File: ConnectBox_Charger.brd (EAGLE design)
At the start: 65 x 30 mm, 6 parts, among them J1 CONNECTOR_PI_40_PIN, J2 Lithium Cell, J3 microUSB Power In, J4 FTDI Serial, J5 5V Charger Output, U1 LTC4040

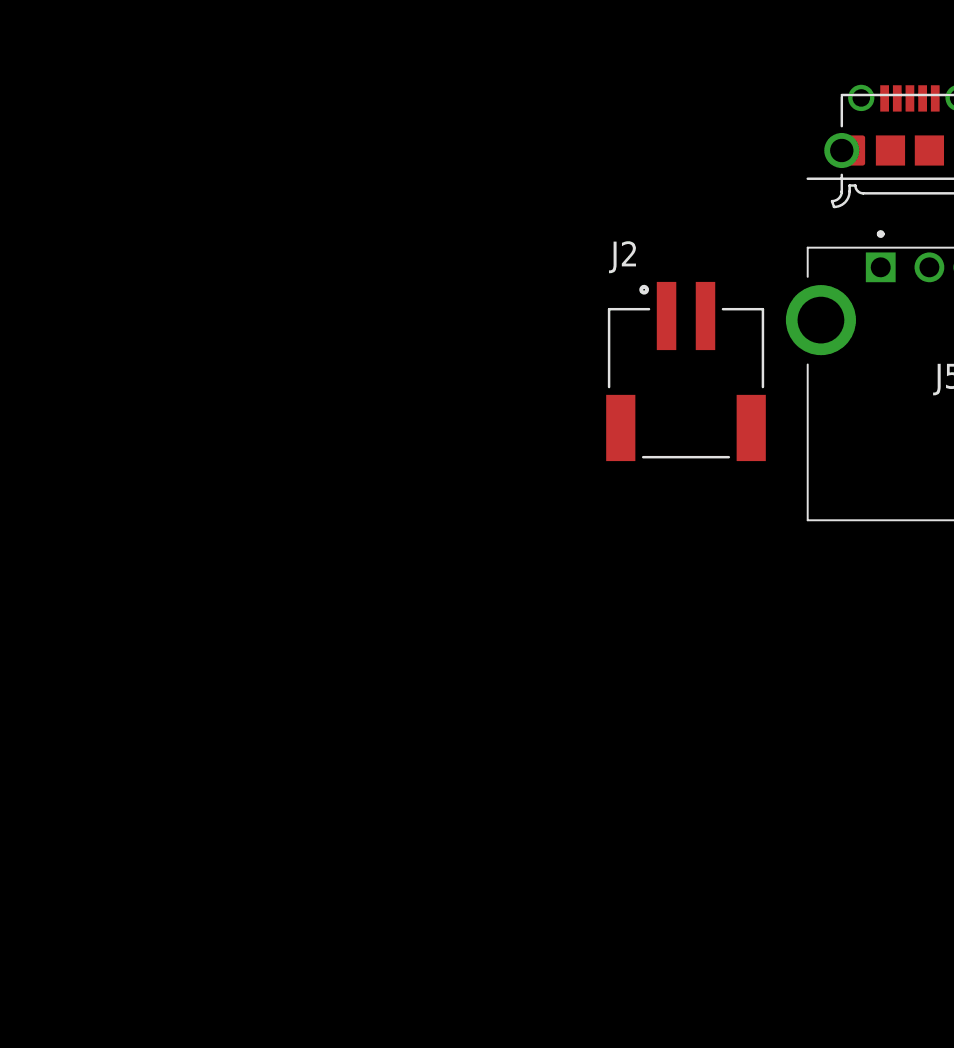
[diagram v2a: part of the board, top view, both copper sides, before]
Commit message: Add parts to library, Schematic. Add LTC4040 IC, inductor, 4x DIP switch, table of settings for Battery Chemistry, charging Voltage.
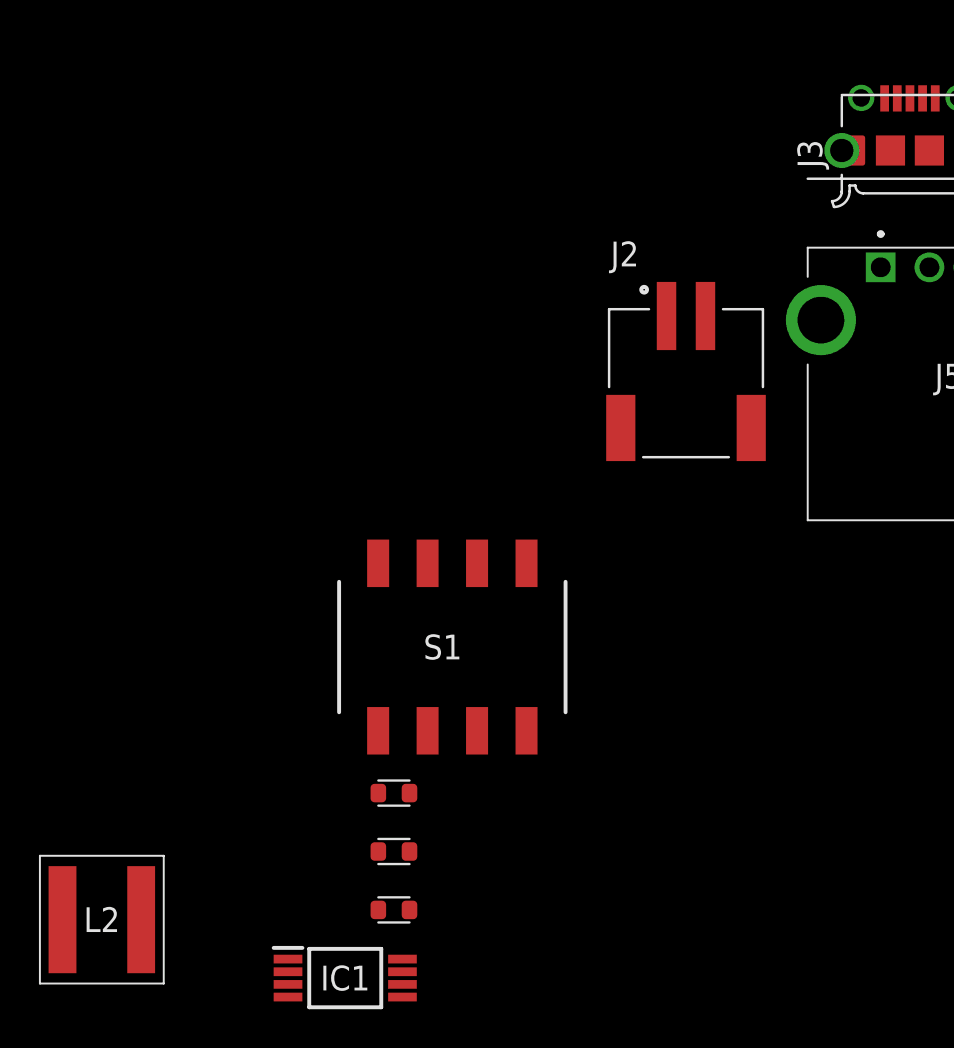
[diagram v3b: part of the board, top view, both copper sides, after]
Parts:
- added IC1: M24C32-RDW6TP, ConnectBox_2019:SOP65P640X120-8N
- added L2: XAL6030-182MEB, ConnectBox_2019:XAL6030182MEB
- added R1, R2, R3: (no value), ConnectBox_2019:RESC1608X55L25N
- added S1: configuration switches, ConnectBox_2019:219-4LPST
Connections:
- new net F0: R3.2, S1.3, U1.14
- new net F1: R2.2, S1.2, U1.13
- new net F2: R1.2, S1.1, U1.12
- net +5V: now also J1.2, J1.4
- net GND: now also R1.1, R2.1, R3.1, U1.17
- net V_IN: now also S1.5, S1.6, S1.7
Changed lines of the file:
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@@
 <attribute name="MF" value="FCI" x="-17.5" y="-25" size="1.778" layer="27" display="off"/>
 <attribute name="MP" value="10118194-0001LF" x="-17.5" y="-25" size="1.778" layer="27" display="off"/>
+<attribute name="NAME" x="-17.5" y="-24.365" size="2.54" layer="51" align="center"/>
 <attribute name="NAME" x="-22" y="-25.9" size="1.27" layer="25" rot="R90"/>
-<attribute name="NAME" x="-17.5" y="-24.365" size="2.54" layer="51" align="center"/>
 <attribute name="PACKAGE" value="DIP-4 FCI" x="-17.5" y="-25" size="1.778" layer="27" display="off"/>
 <attribute name="PRICE" value="0.24 USD" x="-17.5" y="-25" size="1.778" layer="27" display="off"/>
@@
 <attribute name="VALUE" x="-32.75341875" y="-43.6187" size="1.274540625" layer="27"/>
 </element>
+<element name="S1" library="ConnectBox_2019" package="219-4LPST" value="configuration switches" x="-41" y="-50.5" smashed="yes">
+<attribute name="DESCRIPTION" value="Series 219, SMD DIP-switch" x="-41" y="-50.5" size="1.778" layer="27" display="off"/>
+<attribute name="HEIGHT" value="mm" x="-41" y="-50.5" size="1.778" layer="27" display="off"/>
+<attribute name="MANUFACTURER_NAME" value="CTS" x="-41" y="-50.5" size="1.778" layer="27" display="off"/>
+<attribute name="MANUFACTURER_PART_NUMBER" value="219-4LPST" x="-41" y="-50.5" size="1.778" layer="27" display="off"/>
+<attribute name="MOUSER_PART_NUMBER" value="774-2194LPST" x="-41" y="-50.5" size="1.778" layer="27" display="off"/>
+<attribute name="MOUSER_PRICE-STOCK" value="https://www.mouser.com/Search/Refine.aspx?Keyword=774-2194LPST" x="-41" y="-50.5" size="1.778" layer="27" display="off"/>
+<attribute name="NAME" x="-41.492" y="-50.498" size="1.27" layer="25" align="center"/>
+<attribute name="RS_PART_NUMBER" value="1774220" x="-41" y="-50.5" size="1.778" layer="27" display="off"/>
+<attribute name="RS_PRICE-STOCK" value="http://uk.rs-online.com/web/p/products/1774220" x="-41" y="-50.5" size="1.778" layer="27" display="off"/>
+<attribute name="VALUE" x="-41.492" y="-50.498" size="1.27" layer="27" align="center"/>
+</element>
+<element name="R1" library="ConnectBox_2019" package="RESC1608X55L25N" value="" x="-44" y="-58" smashed="yes">
+<attribute name="NAME" x="-42.222" y="-58" size="1.524" layer="25" font="vector" ratio="10" align="center"/>
+<attribute name="NAME" x="-44" y="-58" size="1.016" layer="51" ratio="10" align="center"/>
+</element>
+<element name="R2" library="ConnectBox_2019" package="RESC1608X55L25N" value="" x="-44" y="-61" smashed="yes">
+<attribute name="NAME" x="-42.222" y="-61" size="1.524" layer="25" font="vector" ratio="10" align="center"/>
+<attribute name="NAME" x="-44" y="-61" size="1.016" layer="51" ratio="10" align="center"/>
+</element>
+<element name="R3" library="ConnectBox_2019" package="RESC1608X55L25N" value="" x="-44" y="-64" smashed="yes">
+<attribute name="NAME" x="-42.222" y="-64" size="1.524" layer="25" font="vector" ratio="10" align="center"/>
+<attribute name="NAME" x="-44" y="-64" size="1.016" layer="51" ratio="10" align="center"/>
+</element>
+<element name="IC1" library="ConnectBox_2019" package="SOP65P640X120-8N" value="M24C32-RDW6TP" x="-46.5" y="-67.5" smashed="yes">
+<attribute name="DESCRIPTION" value="STMICROELECTRONICS - M24C32-RDW6TP - EEPROM, 32KBIT, I2C, 1MHZ, TSSOP-8" x="-46.5" y="-67.5" size="1.778" layer="27" display="off"/>
+<attribute name="HEIGHT" value="1.2mm" x="-46.5" y="-67.5" size="1.778" layer="27" display="off"/>
+<attribute name="MANUFACTURER_NAME" value="STMicroelectronics" x="-46.5" y="-67.5" size="1.778" layer="27" display="off"/>
+<attribute name="MANUFACTURER_PART_NUMBER" value="M24C32-RDW6TP" x="-46.5" y="-67.5" size="1.778" layer="27" display="off"/>
+<attribute name="MOUSER_PART_NUMBER" value="511-M24C32-RDW6TP" x="-46.5" y="-67.5" size="1.778" layer="27" display="off"/>
+<attribute name="MOUSER_PRICE-STOCK" value="https://www.mouser.com/Search/Refine.aspx?Keyword=511-M24C32-RDW6TP" x="-46.5" y="-67.5" size="1.778" layer="27" display="off"/>
+<attribute name="NAME" x="-46.5" y="-67.5" size="1.27" layer="25" align="center"/>
+<attribute name="RS_PART_NUMBER" value="" x="-46.5" y="-67.5" size="1.778" layer="27" display="off"/>
+<attribute name="RS_PRICE-STOCK" value="" x="-46.5" y="-67.5" size="1.778" layer="27" display="off"/>
+<attribute name="VALUE" x="-46.5" y="-67.5" size="1.27" layer="27" align="center"/>
+</element>
+<element name="L2" library="ConnectBox_2019" package="XAL6030182MEB" value="XAL6030-182MEB" x="-59" y="-64.5" smashed="yes">
+<attribute name="DESCRIPTION" value="Fixed Inductors 1.8uH 20% 14A 10.52mOhms AEC-Q200" x="-59" y="-64.5" size="1.778" layer="27" display="off"/>
+<attribute name="HEIGHT" value="3.1mm" x="-59" y="-64.5" size="1.778" layer="27" display="off"/>
+<attribute name="MANUFACTURER_NAME" value="COILCRAFT" x="-59" y="-64.5" size="1.778" layer="27" display="off"/>
+<attribute name="MANUFACTURER_PART_NUMBER" value="XAL6030-182MEB" x="-59" y="-64.5" size="1.778" layer="27" display="off"/>
+<attribute name="MOUSER_PART_NUMBER" value="994-XAL6030-182MEB" x="-59" y="-64.5" size="1.778" layer="27" display="off"/>
+<attribute name="MOUSER_PRICE-STOCK" value="https://www.mouser.com/Search/Refine.aspx?Keyword=994-XAL6030-182MEB" x="-59" y="-64.5" size="1.778" layer="27" display="off"/>
+<attribute name="NAME" x="-59" y="-64.5" size="1.27" layer="25" align="center"/>
+<attribute name="RS_PART_NUMBER" value="" x="-59" y="-64.5" size="1.778" layer="27" display="off"/>
+<attribute name="RS_PRICE-STOCK" value="" x="-59" y="-64.5" size="1.778" layer="27" display="off"/>
+<attribute name="VALUE" x="-59" y="-64.5" size="1.27" layer="27" align="center"/>
+</element>
 </elements>
 <signals>
@@
 <contactref element="J5" pad="4"/>
 <contactref element="J2" pad="2"/>
-<wire x1="38.85" y1="25.23" x2="56.63" y2="25.23" width="0" layer="19" extent="1-1"/>
-<wire x1="18.53" y1="25.23" x2="38.85" y2="25.23" width="0" layer="19" extent="1-1"/>
-<wire x1="-20.5" y1="-0.5" x2="18.53" y2="25.23" width="0" layer="19" extent="1-1"/>
-<wire x1="-20.5" y1="-12" x2="-20.5" y2="-0.5" width="0" layer="19" extent="1-1"/>
-<wire x1="-16.2" y1="-22.325" x2="-20.5" y2="-12" width="0" layer="19" extent="1-1"/>
-<wire x1="-12" y1="-31" x2="-16.2" y2="-22.325" width="0" layer="19" extent="1-1"/>
-<wire x1="-8.93" y1="-33.71" x2="-12" y2="-31" width="0" layer="19" extent="1-1"/>
-<wire x1="-28" y1="-33.5" x2="-22.07" y2="-33.71" width="0" layer="19" extent="1-1"/>
+<contactref element="U1" pad="17"/>
+<contactref element="R3" pad="1"/>
+<contactref element="R2" pad="1"/>
+<contactref element="R1" pad="1"/>
+<wire x1="-44.8" y1="-61" x2="-44.8" y2="-64" width="0" layer="19" extent="1-1"/>
+<wire x1="-44.8" y1="-58" x2="-44.8" y2="-61" width="0" layer="19" extent="1-1"/>
+<wire x1="-28" y1="-33.5" x2="-44.8" y2="-58" width="0" layer="19" extent="1-1"/>
+<wire x1="-22.07" y1="-33.71" x2="-28" y2="-33.5" width="0" layer="19" extent="1-1"/>
+<wire x1="-12" y1="-31" x2="-8.93" y2="-33.71" width="0" layer="19" extent="1-1"/>
+<wire x1="-16.2" y1="-22.325" x2="-12" y2="-31" width="0" layer="19" extent="1-1"/>
+<wire x1="-20.5" y1="-12" x2="-16.2" y2="-22.325" width="0" layer="19" extent="1-1"/>
+<wire x1="-20.5" y1="-0.5" x2="-20.5" y2="-12" width="0" layer="19" extent="1-1"/>
+<wire x1="-18.565" y1="0" x2="-20.5" y2="-0.5" width="0" layer="19" extent="1-1"/>
+<wire x1="18.53" y1="25.23" x2="-18.565" y2="0" width="0" layer="19" extent="1-1"/>
+<wire x1="38.85" y1="25.23" x2="18.53" y2="25.23" width="0" layer="19" extent="1-1"/>
+<wire x1="56.63" y1="25.23" x2="38.85" y2="25.23" width="0" layer="19" extent="1-1"/>
 </signal>
 <signal name="TO_PI">
@@
 <signal name="V_IN">
 <contactref element="J3" pad="1"/>
+<contactref element="S1" pad="7"/>
+<contactref element="S1" pad="5"/>
+<contactref element="S1" pad="6"/>
+<wire x1="-39.73" y1="-46.2" x2="-42.27" y2="-46.2" width="0" layer="19" extent="1-1"/>
+<wire x1="-37.19" y1="-46.2" x2="-39.73" y2="-46.2" width="0" layer="19" extent="1-1"/>
+<wire x1="-18.8" y1="-22.325" x2="-37.19" y2="-46.2" width="0" layer="19" extent="1-1"/>
 </signal>
 <signal name="+5V">
 <contactref element="J5" pad="1"/>
+<contactref element="J1" pad="4"/>
+<contactref element="J1" pad="2"/>
+<wire x1="8.37" y1="27.77" x2="-19" y2="-31" width="0" layer="19" extent="1-1"/>
+<wire x1="10.91" y1="27.77" x2="8.37" y2="27.77" width="0" layer="19" extent="1-1"/>
 </signal>
 <signal name="BATT">
 <contactref element="J2" pad="1"/>
 </signal>
+<signal name="F2">
+<contactref element="U1" pad="12"/>
+<contactref element="S1" pad="1"/>
+<contactref element="R1" pad="2"/>
+<wire x1="-44.81" y1="-54.8" x2="-43.2" y2="-58" width="0" layer="19" extent="1-1"/>
+<wire x1="-19.5" y1="-2.935" x2="-44.81" y2="-54.8" width="0" layer="19" extent="1-1"/>
+</signal>
+<signal name="F1">
+<contactref element="U1" pad="13"/>
+<contactref element="S1" pad="2"/>
+<contactref element="R2" pad="2"/>
+<wire x1="-42.27" y1="-54.8" x2="-43.2" y2="-61" width="0" layer="19" extent="1-1"/>
+<wire x1="-18.565" y1="-2" x2="-42.27" y2="-54.8" width="0" layer="19" extent="1-1"/>
+</signal>
+<signal name="F0">
+<contactref element="U1" pad="14"/>
+<contactref element="R3" pad="2"/>
+<contactref element="S1" pad="3"/>
+<wire x1="-39.73" y1="-54.8" x2="-43.2" y2="-64" width="0" layer="19" extent="1-1"/>
+<wire x1="-18.565" y1="-1.5" x2="-39.73" y2="-54.8" width="0" layer="19" extent="1-1"/>
+</signal>
 </signals>

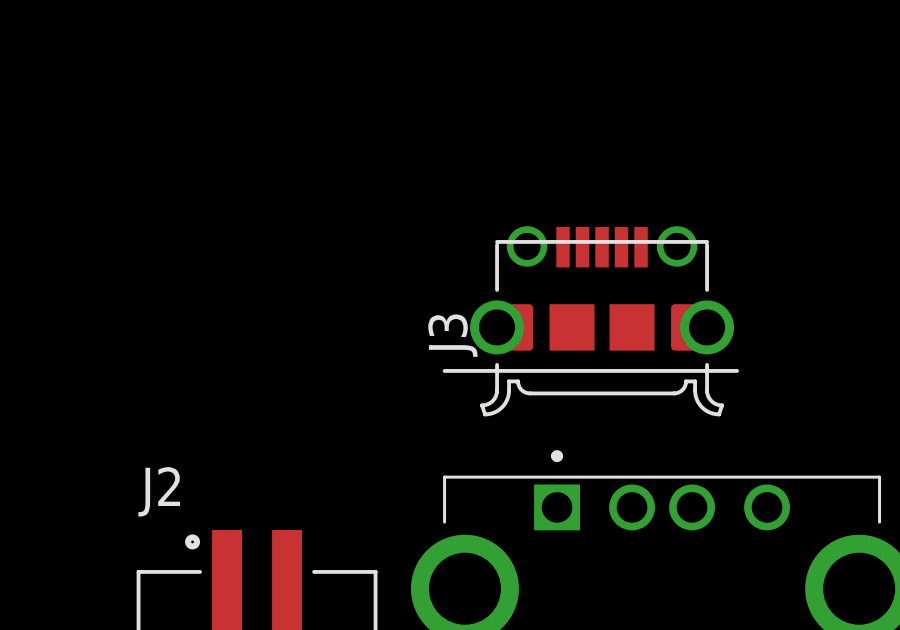
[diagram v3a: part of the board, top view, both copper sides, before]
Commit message: Update LTC4040 and Pi 40-pin connector to 0.1" pin spacing versions to save space on schematic.
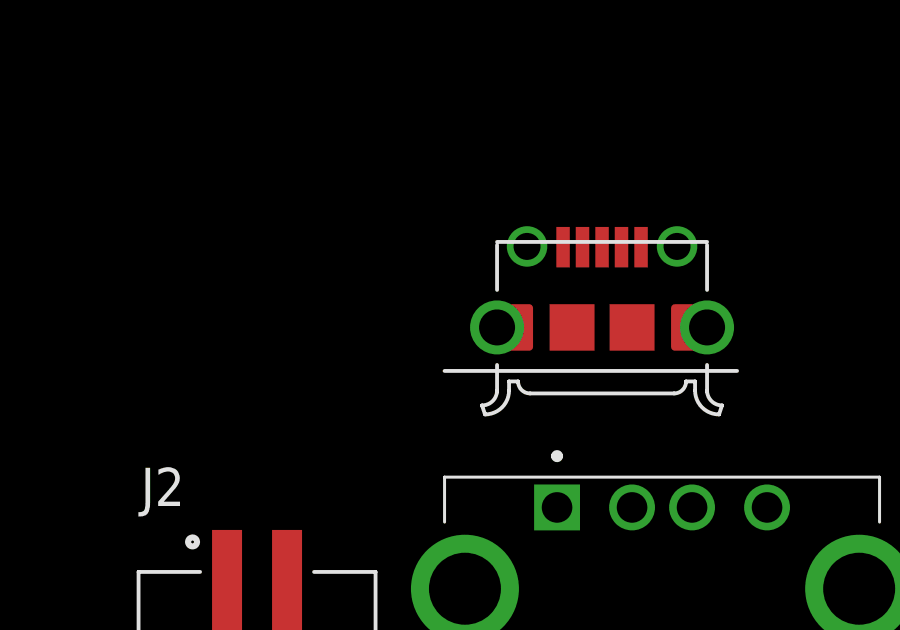
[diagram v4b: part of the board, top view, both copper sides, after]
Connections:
- net +5V: now also S1.5, S1.6, S1.7, U1.24
- net F0: no longer U1.14
- net F1: no longer U1.13
- net F2: no longer U1.12
- net GND: no longer J1.25, J1.39, J1.9, U1.17
- net V_IN: no longer S1.5, S1.6, S1.7
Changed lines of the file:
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@@
 <attribute name="MF" value="FCI" x="-17.5" y="-25" size="1.778" layer="27" display="off"/>
 <attribute name="MP" value="10118194-0001LF" x="-17.5" y="-25" size="1.778" layer="27" display="off"/>
+<attribute name="NAME" x="-22" y="-25.9" size="1.27" layer="25" rot="R90"/>
 <attribute name="NAME" x="-17.5" y="-24.365" size="2.54" layer="51" align="center"/>
-<attribute name="NAME" x="-22" y="-25.9" size="1.27" layer="25" rot="R90"/>
 <attribute name="PACKAGE" value="DIP-4 FCI" x="-17.5" y="-25" size="1.778" layer="27" display="off"/>
 <attribute name="PRICE" value="0.24 USD" x="-17.5" y="-25" size="1.778" layer="27" display="off"/>
@@
 <signal name="GND">
 <contactref element="J4" pad="1"/>
-<contactref element="J1" pad="39"/>
-<contactref element="J1" pad="25"/>
-<contactref element="J1" pad="9"/>
-<contactref element="U1" pad="25"/>
 <contactref element="J3" pad="5"/>
 <contactref element="J5" pad="MH2" route="any" routetag="G$1.SHIELD"/>
@@
 <contactref element="J5" pad="4"/>
 <contactref element="J2" pad="2"/>
-<contactref element="U1" pad="17"/>
 <contactref element="R3" pad="1"/>
 <contactref element="R2" pad="1"/>
 <contactref element="R1" pad="1"/>
+<contactref element="U1" pad="25"/>
 <wire x1="-44.8" y1="-61" x2="-44.8" y2="-64" width="0" layer="19" extent="1-1"/>
 <wire x1="-44.8" y1="-58" x2="-44.8" y2="-61" width="0" layer="19" extent="1-1"/>
@@
 <wire x1="-20.5" y1="-12" x2="-16.2" y2="-22.325" width="0" layer="19" extent="1-1"/>
 <wire x1="-20.5" y1="-0.5" x2="-20.5" y2="-12" width="0" layer="19" extent="1-1"/>
-<wire x1="-18.565" y1="0" x2="-20.5" y2="-0.5" width="0" layer="19" extent="1-1"/>
-<wire x1="18.53" y1="25.23" x2="-18.565" y2="0" width="0" layer="19" extent="1-1"/>
-<wire x1="38.85" y1="25.23" x2="18.53" y2="25.23" width="0" layer="19" extent="1-1"/>
-<wire x1="56.63" y1="25.23" x2="38.85" y2="25.23" width="0" layer="19" extent="1-1"/>
 </signal>
 <signal name="TO_PI">
@@
 <signal name="V_IN">
 <contactref element="J3" pad="1"/>
+</signal>
+<signal name="+5V">
+<contactref element="J5" pad="1"/>
+<contactref element="J1" pad="4"/>
+<contactref element="J1" pad="2"/>
+<contactref element="U1" pad="24"/>
 <contactref element="S1" pad="7"/>
 <contactref element="S1" pad="5"/>
@@
 <wire x1="-39.73" y1="-46.2" x2="-42.27" y2="-46.2" width="0" layer="19" extent="1-1"/>
 <wire x1="-37.19" y1="-46.2" x2="-39.73" y2="-46.2" width="0" layer="19" extent="1-1"/>
-<wire x1="-18.8" y1="-22.325" x2="-37.19" y2="-46.2" width="0" layer="19" extent="1-1"/>
-</signal>
-<signal name="+5V">
-<contactref element="J5" pad="1"/>
-<contactref element="J1" pad="4"/>
-<contactref element="J1" pad="2"/>
-<wire x1="8.37" y1="27.77" x2="-19" y2="-31" width="0" layer="19" extent="1-1"/>
+<wire x1="-19" y1="-31" x2="-37.19" y2="-46.2" width="0" layer="19" extent="1-1"/>
+<wire x1="-21.5" y1="1.935" x2="-19" y2="-31" width="0" layer="19" extent="1-1"/>
+<wire x1="8.37" y1="27.77" x2="-21.5" y2="1.935" width="0" layer="19" extent="1-1"/>
 <wire x1="10.91" y1="27.77" x2="8.37" y2="27.77" width="0" layer="19" extent="1-1"/>
 </signal>
@@
 </signal>
 <signal name="F2">
-<contactref element="U1" pad="12"/>
 <contactref element="S1" pad="1"/>
 <contactref element="R1" pad="2"/>
 <wire x1="-44.81" y1="-54.8" x2="-43.2" y2="-58" width="0" layer="19" extent="1-1"/>
-<wire x1="-19.5" y1="-2.935" x2="-44.81" y2="-54.8" width="0" layer="19" extent="1-1"/>
 </signal>
 <signal name="F1">
-<contactref element="U1" pad="13"/>
 <contactref element="S1" pad="2"/>
 <contactref element="R2" pad="2"/>
 <wire x1="-42.27" y1="-54.8" x2="-43.2" y2="-61" width="0" layer="19" extent="1-1"/>
-<wire x1="-18.565" y1="-2" x2="-42.27" y2="-54.8" width="0" layer="19" extent="1-1"/>
 </signal>
 <signal name="F0">
-<contactref element="U1" pad="14"/>
 <contactref element="R3" pad="2"/>
 <contactref element="S1" pad="3"/>
 <wire x1="-39.73" y1="-54.8" x2="-43.2" y2="-64" width="0" layer="19" extent="1-1"/>
-<wire x1="-18.565" y1="-1.5" x2="-39.73" y2="-54.8" width="0" layer="19" extent="1-1"/>
 </signal>
 </signals>
